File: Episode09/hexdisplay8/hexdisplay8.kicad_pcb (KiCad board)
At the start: 2 copper layers, 51.9 x 23.8 mm, 20 parts, among them J11 Conn_01x05, J12 Conn_01x05, J21 Conn_01x05, J22 Conn_01x05, J3 Conn_01x02, J4 Conn_01x08, J5 Conn_01x06, Q1 MMBT3906, Q2 MMBT3906, U1 ATTINY2313A-SU

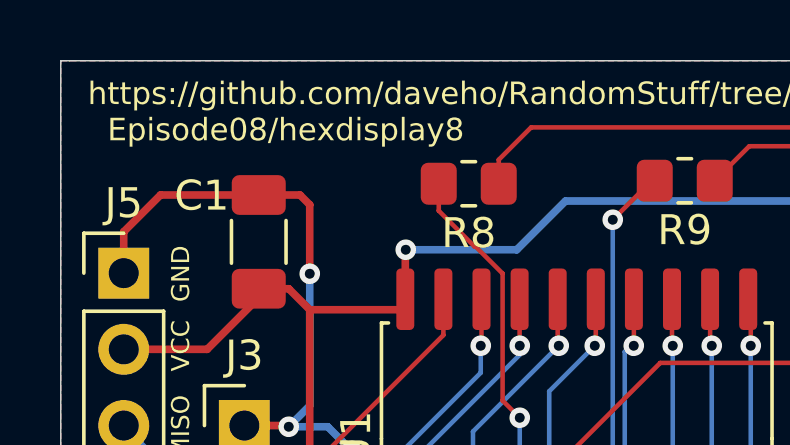
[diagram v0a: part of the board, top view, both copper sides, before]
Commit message: updated URL on silkscreen
The hex display episode will be Random Stuff #9.
Unfortunately, the actual PCBs say Episode 08. Oh well.
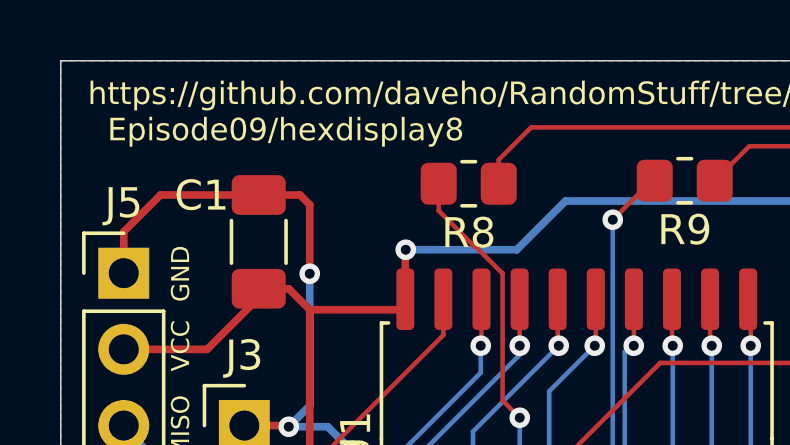
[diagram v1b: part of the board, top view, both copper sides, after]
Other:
- board text added: "https://github.com/daveho/RandomStuff/tree/master/ Episode09/hexdisplay8"
- board text removed: "https://github.com/daveho/RandomStuff/tree/master/ Episode08/hexdisplay8"
